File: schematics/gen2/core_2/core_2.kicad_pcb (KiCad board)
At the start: 2 copper layers, 100 x 91.1 mm, 24 parts, among them U1 74LS04, U2 74LS574, U3 74LS02, U5 74LS00

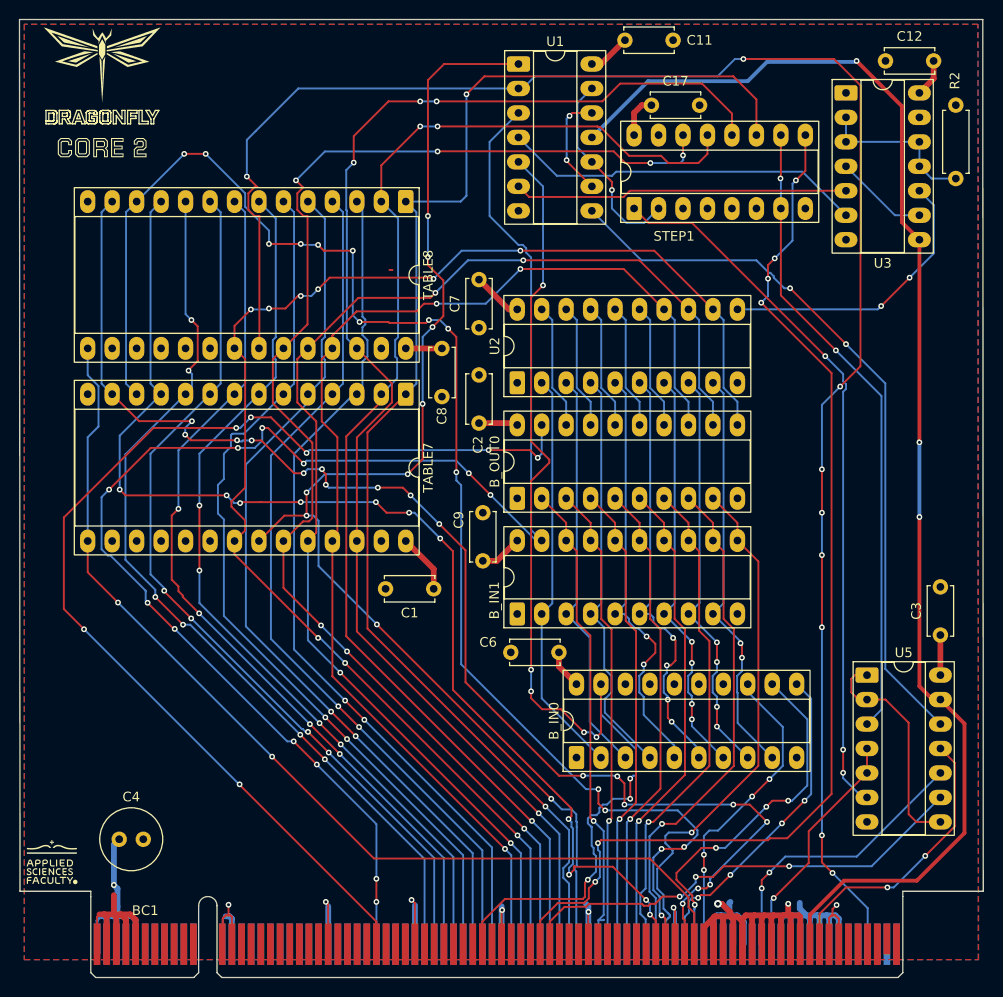
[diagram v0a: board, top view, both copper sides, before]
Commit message: fix(kicad): vcc zones
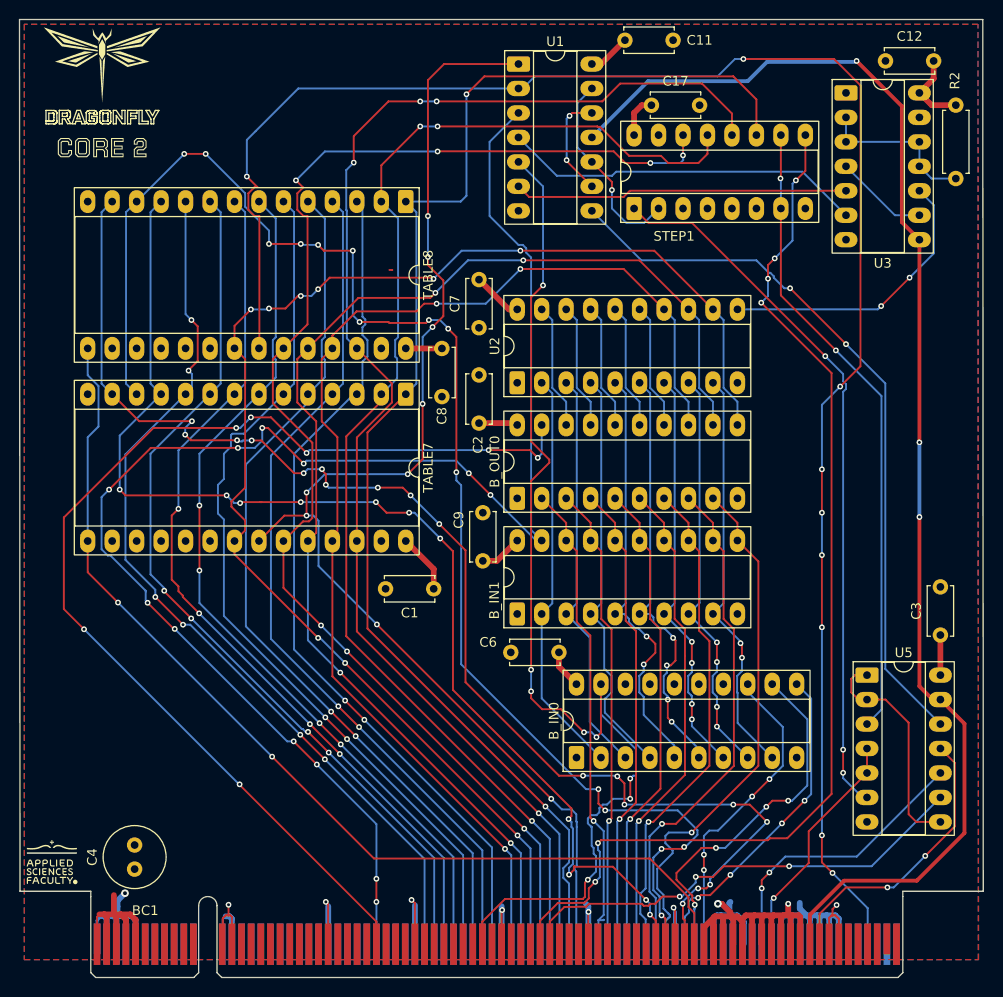
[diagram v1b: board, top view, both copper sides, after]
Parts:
- moved C4 3.49 mm to (196.8, 100.3), turned to 90 degrees
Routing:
- net VCC: track 93.4 -> 92.0 mm
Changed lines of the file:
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@@
 			(pinfunction "VCC")
 			(pintype "power_in")
+			(zone_connect 0)
 		)
 		(embedded_fonts no)
@@
 	(footprint "Capacitor_THT:C_Radial_D6.3mm_H5.0mm_P2.50mm"
 		(layer "F.Cu")
-		(at 195.25 97.2)
+		(at 196.85 100.3 90)
 		(descr "C, Radial series, Radial, pin pitch=2.50mm, diameter=6.3mm, height=5mm, Non-Polar Electrolytic Capacitor")
 		(tags "C Radial series Radial pin pitch 2.50mm diameter 6.3mm height 5mm Non-Polar Electrolytic Capacitor")
 		(property "Reference" "C4"
-			(at 1.25 -4.4 0)
+			(at 1.25 -4.4 90)
 			(layer "F.SilkS")
 			(effects
@@
 		)
 		(property "Value" "C"
-			(at 1.25 4.4 0)
+			(at 1.25 4.4 90)
 			(layer "F.Fab")
 			(effects
@@
 		)
 		(property "Datasheet" "~"
-			(at 0 0 0)
+			(at 0 0 90)
 			(layer "F.Fab")
 			(hide yes)
@@
 		)
 		(property "Description" "Unpolarized capacitor"
-			(at 0 0 0)
+			(at 0 0 90)
 			(layer "F.Fab")
 			(hide yes)
@@
 		)
 		(fp_text user "${REFERENCE}"
-			(at 1.25 0 0)
+			(at 1.25 0 90)
 			(layer "F.Fab")
 			(effects
@@
 		)
 		(pad "1" thru_hole circle
-			(at 0 0)
+			(at 0 0 90)
 			(size 1.6 1.6)
 			(drill 0.8)
@@
 		)
 		(pad "2" thru_hole circle
-			(at 2.5 0)
+			(at 2.5 0 90)
 			(size 1.6 1.6)
 			(drill 0.8)
@@
 			(pinfunction "VCC")
 			(pintype "power_in")
+			(zone_connect 0)
 		)
 		(embedded_fonts no)
@@
 			(pinfunction "VCC")
 			(pintype "power_in")
+			(zone_connect 0)
 		)
 		(embedded_fonts no)
@@
 			(pinfunction "VCC")
 			(pintype "power_in")
+			(zone_connect 0)
 		)
 		(embedded_fonts no)
@@
 			(pinfunction "VCC")
 			(pintype "power_in")
+			(zone_connect 0)
 		)
 		(embedded_fonts no)
@@
 			(pinfunction "VCC")
 			(pintype "power_in")
+			(zone_connect 0)
 		)
 		(embedded_fonts no)
@@
 			(pinfunction "VCC")
 			(pintype "power_in")
+			(zone_connect 0)
 		)
 		(embedded_fonts no)
@@
 			(pinfunction "VCC")
 			(pintype "power_in")
+			(zone_connect 0)
 		)
 		(embedded_fonts no)
@@
 			(pinfunction "VCC")
 			(pintype "power_in")
+			(zone_connect 0)
 		)
 		(embedded_fonts no)
@@
 			(pinfunction "VCC")
 			(pintype "power_in")
+			(zone_connect 0)
 		)
 		(embedded_fonts no)
@@
 	)
 	(segment
+		(start 282.1 20.99)
+		(end 279.59 20.99)
+		(width 0.6)
+		(layer "F.Cu")
+		(net 6)
+	)
+	(segment
 		(start 194.7 105)
 		(end 194.7 103)
@@
 	)
 	(segment
+		(start 279.59 20.99)
+		(end 278.32 19.72)
+		(width 0.6)
+		(layer "F.Cu")
+		(net 6)
+	)
+	(segment
 		(start 236.38 54)
 		(end 236.57 54.19)
@@
 	)
 	(via
-		(at 194.7 101.95)
-		(size 0.6)
-		(drill 0.3)
+		(at 195.85 102.8)
+		(size 0.8)
+		(drill 0.4)
 		(layers "F.Cu" "B.Cu")
 		(net 6)
@@
 	)
 	(segment
-		(start 195.075 104.175)
-		(end 195.075 102.325)
-		(width 0.6)
-		(layer "B.Cu")
-		(net 6)
-	)
-	(segment
-		(start 194.7 97.75)
-		(end 195.25 97.2)
+		(start 195.075 105.175)
+		(end 195.075 104.175)
 		(width 0.6)
 		(layer "B.Cu")
@@
 	)
 	(segment
-		(start 195.075 105.175)
-		(end 195.075 104.175)
+		(start 195.075 103.575)
+		(end 195.85 102.8)
 		(width 0.6)
 		(layer "B.Cu")
@@
 	)
 	(segment
+		(start 195.075 104.175)
+		(end 195.075 103.575)
+		(width 0.6)
+		(layer "B.Cu")
+		(net 6)
+	)
+	(segment
 		(start 195.95 105.5)
 		(end 195.625 105.175)
@@
 	)
 	(segment
-		(start 195.075 102.325)
-		(end 194.7 101.95)
-		(width 0.6)
-		(layer "B.Cu")
-		(net 6)
-	)
-	(segment
 		(start 195.075 105.175)
 		(end 195.625 105.175)
@@
 		(width 0.6)
 		(layer "B.Cu")
-		(net 6)
-	)
-	(segment
-		(start 194.7 101.95)
-		(end 194.7 97.75)
-		(width 0.6)
-		(layer "B.Cu")
